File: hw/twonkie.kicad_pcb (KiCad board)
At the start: 4 copper layers, 25.4 x 25.4 mm, 55 parts, among them J1 DX07P024AJ1R1500, J2 690-024-294T331, J3 629105150521, Q1 BSD840N, Q2 BSD840N, Q3 BSD840N, SW1 EVQ-P7M01P, U1 INA260, U2 INA260, U3 MIC5504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

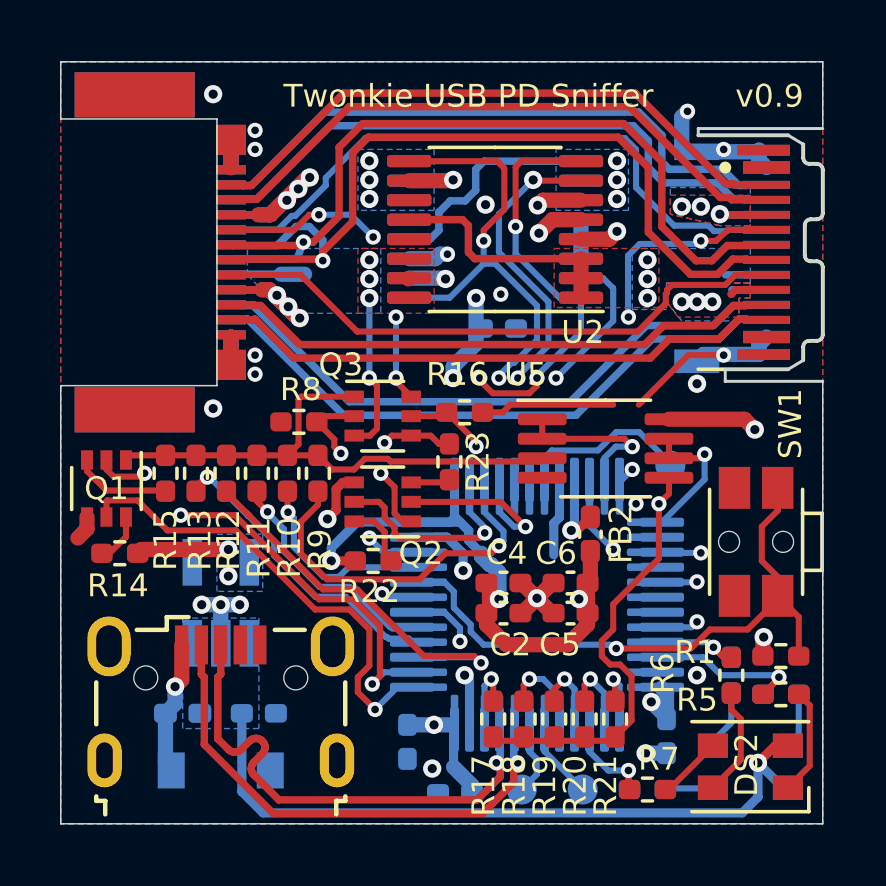
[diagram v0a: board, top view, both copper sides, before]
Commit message: Many reworks based on David's and Vincent's feedback
* The USB plug wouldn't straddle a 1.6mm board, so switched to
  a different one
* Redid the USB section to make room for the new plug
* Twinkie firmware needs some special pin functions I wasn't aware
  of, so some signals had to be moved to different pins
* Misc other tweaks like merging resistor values
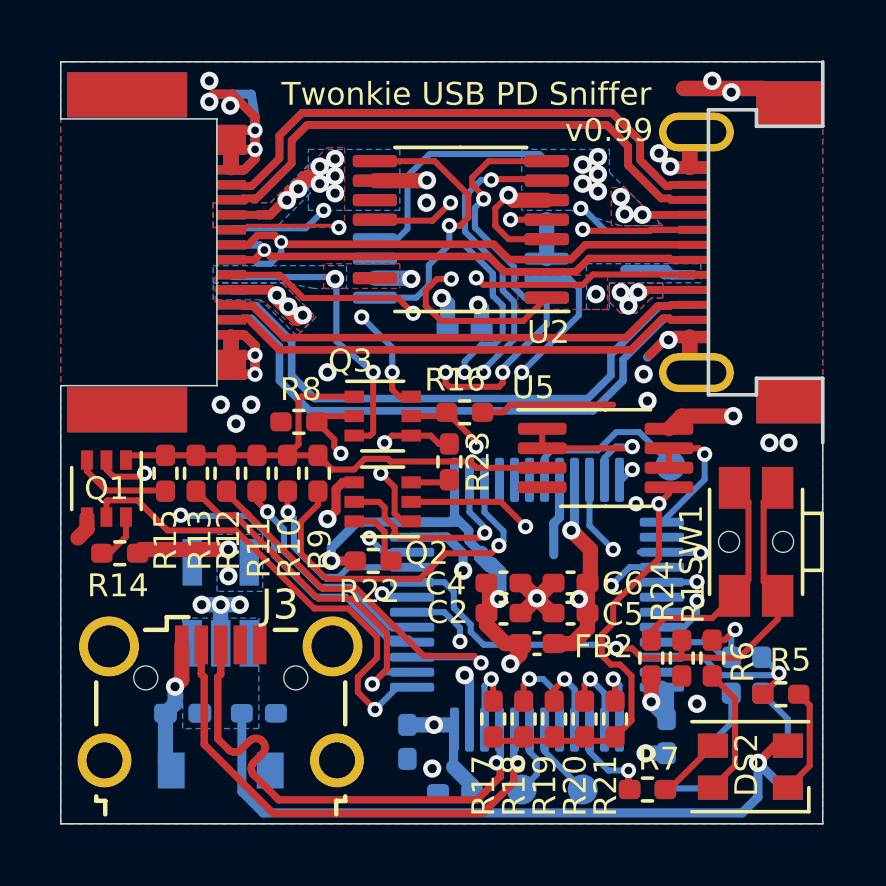
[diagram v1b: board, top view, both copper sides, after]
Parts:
- added R24: 100, Resistor_SMD:R_0402_1005Metric_Pad0.72x0.64mm_HandSolder, F.Cu at (91.6, 54.2)
- J1: value DX07P024AJ1R1500 -> USB4151; footprint twonkie:JAE_DX07P024AJ1R1500 -> twonkie:GCT_USB4151_EdgeMount
- J3: footprint Connector_USB:USB_Micro-B_Wuerth_629105150521 -> Connector_USB:USB_Micro-B_Wuerth_629105150521_CircularHoles
- R1: value 51k1 -> 35k7
- R16, R8: value 301k -> 35k7
- R2, R5: value 806 -> 390
- R3, R6: value 576 -> 240
- R4, R7: value 604 -> 240
- U4: value STM32F042C6 -> STM32F072CB; footprint twonkie:LQFP-48_7x7mm_P0.5mm-QFN48-Frankenstein -> Package_QFP:LQFP-48_7x7mm_P0.5mm
- moved FB2 4.06 mm to (87.8, 53.7), turned to 0 degrees
- moved J1 3.81 mm to (93.5, 40.6)
- moved R1 3.30 mm to (92.6, 54.2), turned to 270 degrees
- moved ? 2.62 mm to (78.0, 34.8)
- moved dojoe-logo 2.11 mm to (85.5, 45.5)
- moved C9 1.14 mm to (85.3, 43.2)
- moved U1 1.14 mm to (85.2, 39.9)
- moved U2 1.14 mm to (85.2, 39.9)
- moved R2 0.90 mm to (95.2, 54.7), turned to 90 degrees
- moved R6 0.85 mm to (93.6, 54.2)
- moved U5 0.32 mm to (90.0, 47.5)
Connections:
- C5 pad 1: +3V3 -> Net-(C5-Pad1)
- C6 pad 1: +3V3 -> Net-(C5-Pad1)
- FB2 pad 2: Net-(FB2-Pad2) -> Net-(C5-Pad1)
- R1 pad 1: +3V3 -> /BOOT
- R1 pad 2: /BOOT -> GND
- SW1 pad 1: GND -> Net-(R24-Pad2)
- U4 pad 16: Net-(U4-Pad16) -> /CC2_TX_DATA
- U4 pad 38: /CC1_TX_DATA -> /CC1_RPUSB
- U4 pad 4: /CC2_TX_DATA -> Net-(U4-Pad4)
- U4 pad 40: /CC1_RPUSB -> /CC1_TX_DATA
- U4 pad 9: Net-(FB2-Pad2) -> Net-(C5-Pad1)
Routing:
- net GND: track 40.9 -> 67.1 mm, vias 26 -> 33
- net /USBC_D-: track 28.6 -> 17.2 mm
- net /USBC_D+: track 27.0 -> 18.4 mm
- net Net-(R24-Pad2): track 0.00 -> 7.83 mm
- net /CC2_PLUG: track 9.46 -> 16.4 mm
- net Net-(C5-Pad1): track 0.00 -> 6.92 mm, vias 0 -> 2
- net /SBU2: track 22.8 -> 17.2 mm, vias 0 -> 2
- net /CC2_TX_DATA: track 6.30 -> 9.77 mm, vias 1 -> 2
- net /SBU1: track 19.7 -> 16.5 mm, vias 0 -> 2
- net /RX2+: track 18.9 -> 16.3 mm
- net /RX2-: track 18.9 -> 16.3 mm
- net Net-(FB2-Pad2): track 2.55 -> 0.00 mm, vias 1 -> 0
- net /TX_CLK: track 17.6 -> 15.4 mm
- net /CC1_RECEP: track 26.0 -> 23.8 mm, vias 6 -> 4
- net /INA_SDA: track 23.7 -> 25.8 mm
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- added copper zone on F.Cu, net /VBUS_RECEP
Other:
- outline, holes or cut-outs redrawn
- net class Diffpair: trace_width 0.24892 -> 0.254
- rule trace_min: 0.1524 -> 0.127
- rule via_min_size: 0.508 -> 0.4572
- board text added: "v0.99"
- board text removed: "v0.9"

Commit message: v0.99 with fabrication files
* Switch USB-MicroB receptacle to version with drill slots
* Expand VBUS connections on USB-C plug
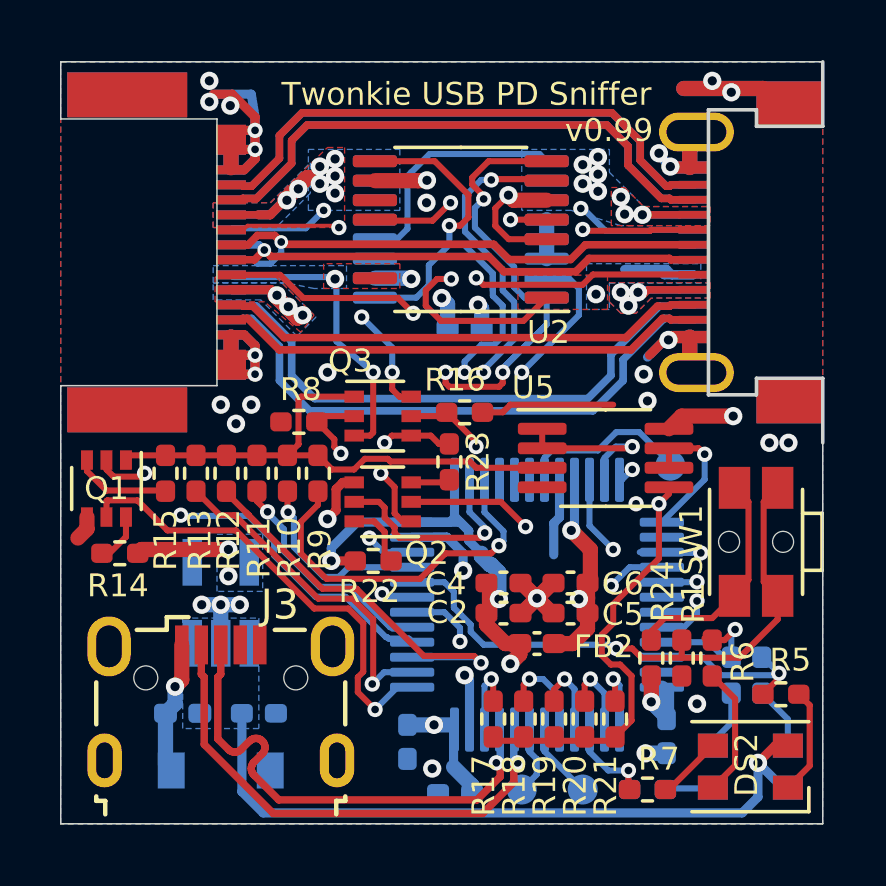
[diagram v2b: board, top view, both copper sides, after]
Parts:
- J3: footprint Connector_USB:USB_Micro-B_Wuerth_629105150521_CircularHoles -> Connector_USB:USB_Micro-B_Wuerth_629105150521

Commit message: First batch of v1.0 fixes
* Restore QFN/TQFP combo footprint for U4, make sure it stays
* Grow some VBUS copper pours
* Make U4 decap ground connections less solid for better soldering
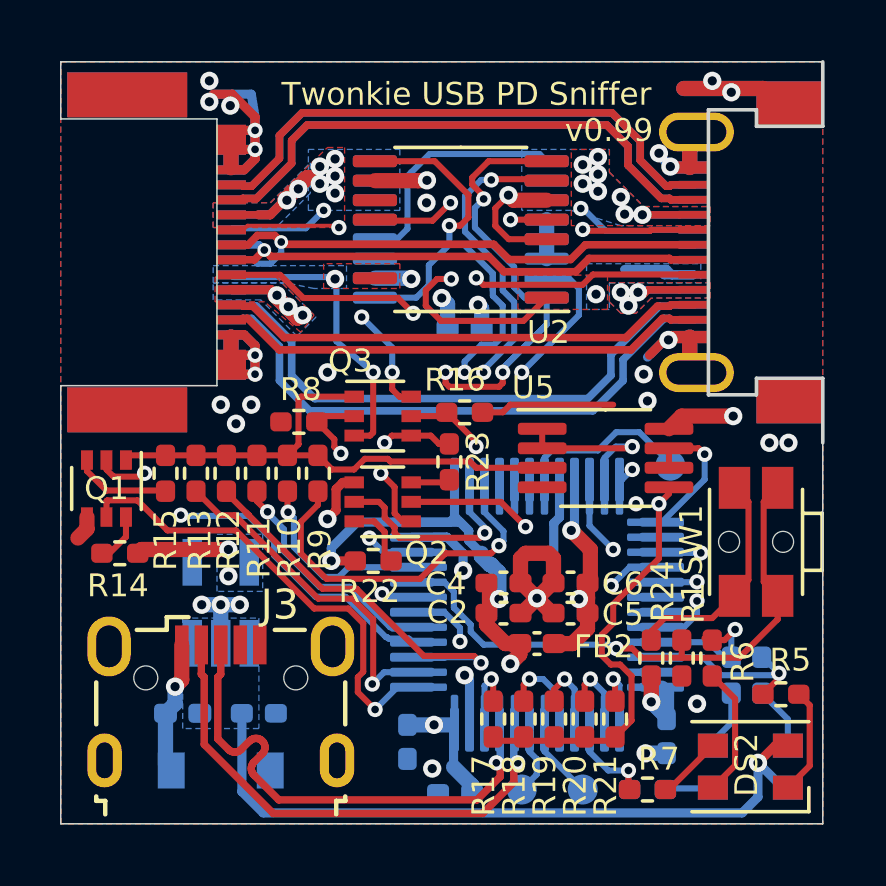
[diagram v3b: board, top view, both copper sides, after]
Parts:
- U4: footprint Package_QFP:LQFP-48_7x7mm_P0.5mm -> twonkie:LQFP-48_7x7mm_P0.5mm-QFN48-Frankenstein
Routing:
- net GND: track 67.1 -> 70.0 mm
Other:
- board text added: "TODO: Corner relief"

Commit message: Add relief to J2 cutout corners, update ground connections
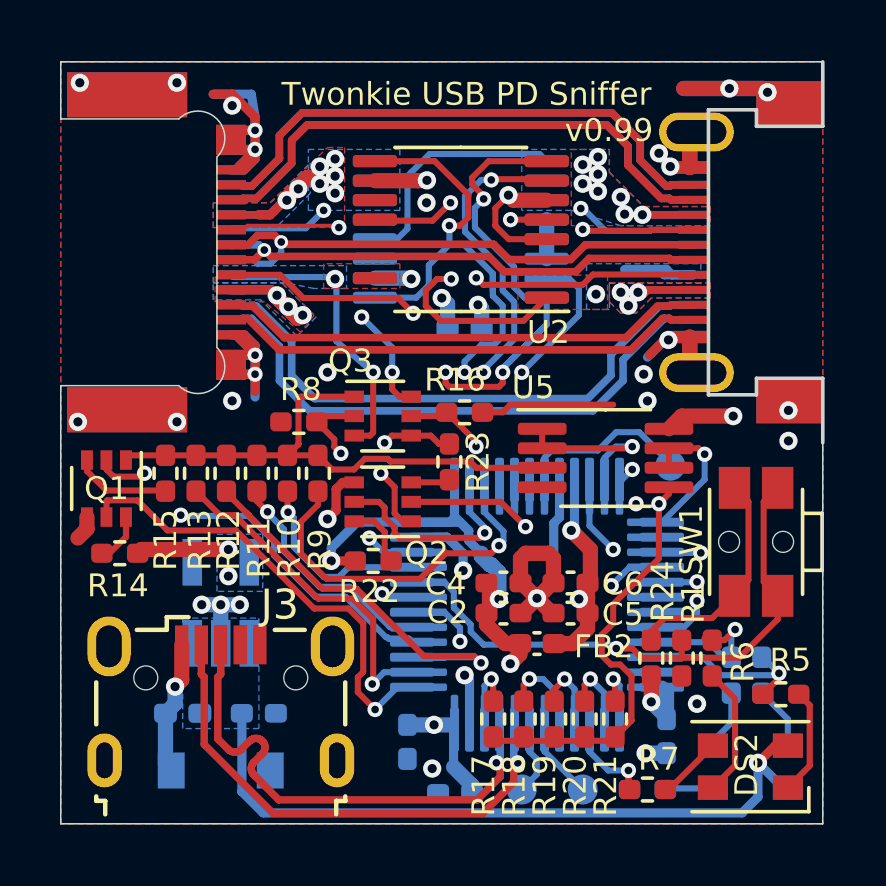
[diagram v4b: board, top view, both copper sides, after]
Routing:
- net GND: track 70.0 -> 68.4 mm
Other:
- outline, holes or cut-outs redrawn
- board text removed: "TODO: Corner relief"

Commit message: Add I2C pullup resistors
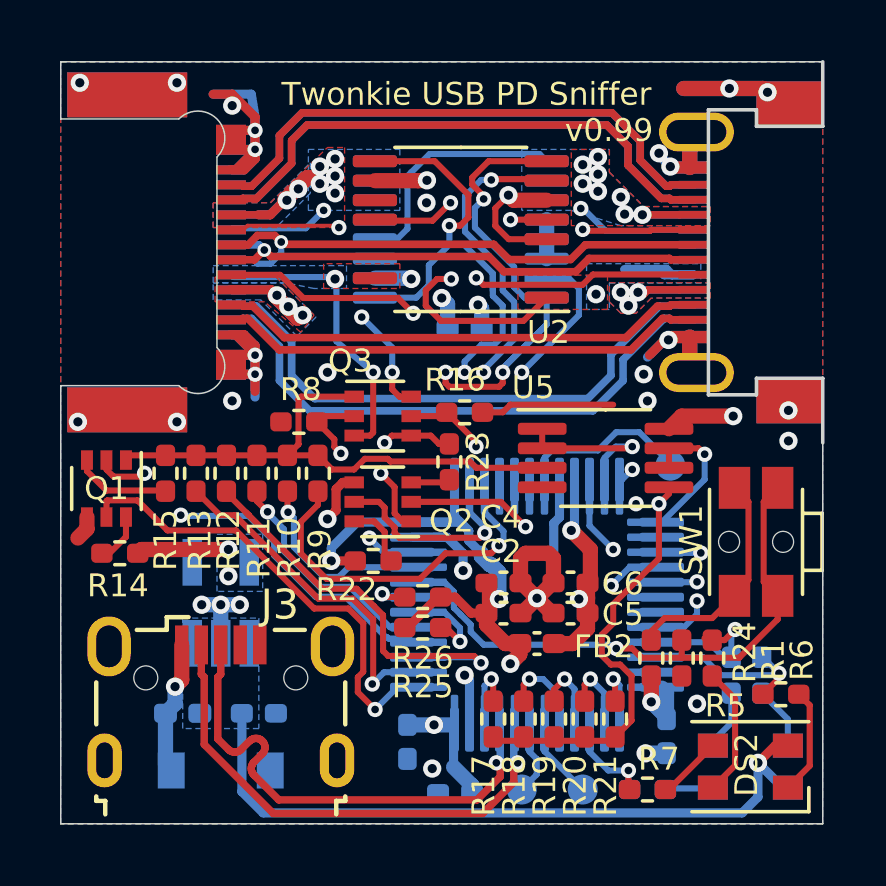
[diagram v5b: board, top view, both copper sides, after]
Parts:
- added R25: 4k75, Resistor_SMD:R_0402_1005Metric_Pad0.72x0.64mm_HandSolder, F.Cu at (83.9, 53.1)
- added R26: 4k75, Resistor_SMD:R_0402_1005Metric_Pad0.72x0.64mm_HandSolder, F.Cu at (83.9, 52.1)
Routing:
- net +3V3: track 43.4 -> 46.8 mm
- net /CC1_RD: track 13.4 -> 14.7 mm
- net /INA_SCL: track 29.3 -> 30.1 mm
- net /INA_SDA: track 25.8 -> 26.6 mm

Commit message: Improve C2/4/5/6 solderability
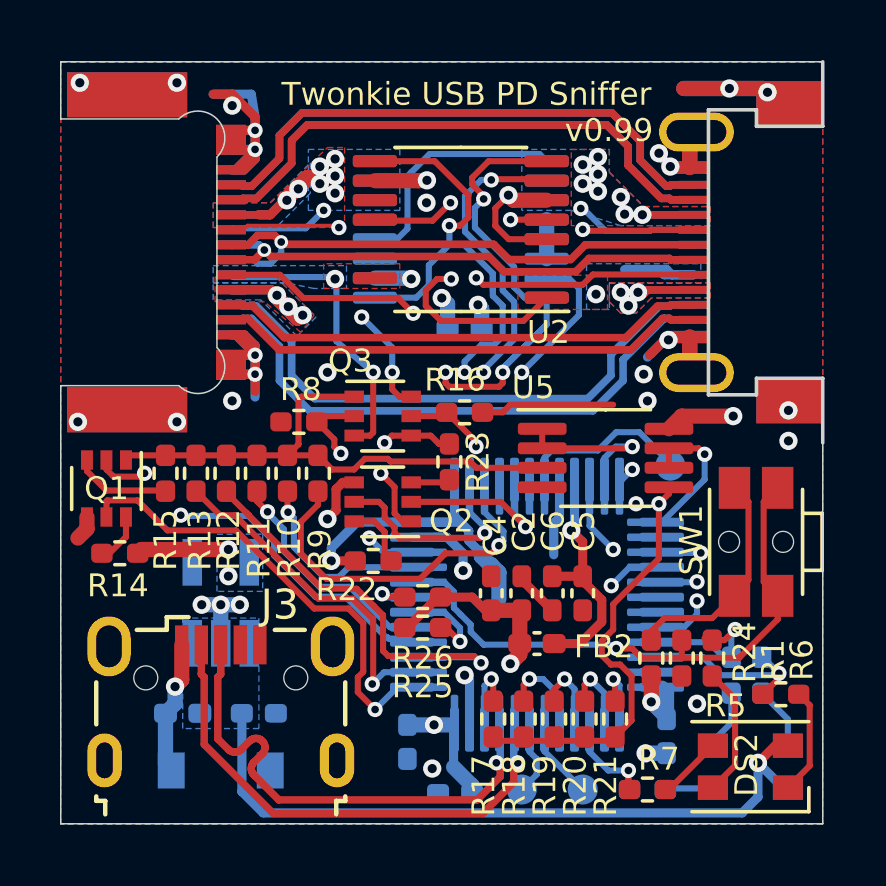
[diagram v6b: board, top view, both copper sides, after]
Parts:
- moved C2 0.90 mm to (87.2, 52.0), turned to 90 degrees
- moved C5 0.78 mm to (89.3, 52.0), turned to 270 degrees
- moved C6 0.70 mm to (88.3, 52.0), turned to 270 degrees
- moved C4 0.53 mm to (86.2, 52.0), turned to 90 degrees
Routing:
- net GND: track 68.4 -> 64.1 mm, vias 33 -> 32
- net +3V3: track 46.8 -> 45.0 mm, vias 13 -> 12
- net Net-(C5-Pad1): track 6.92 -> 8.10 mm, vias 2 -> 1

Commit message: Solderability improvememts around J3
* Extend J3 pads for easier hand soldering
* Move FB1, C1 to reach pads better
* Move J3 closer to board edge
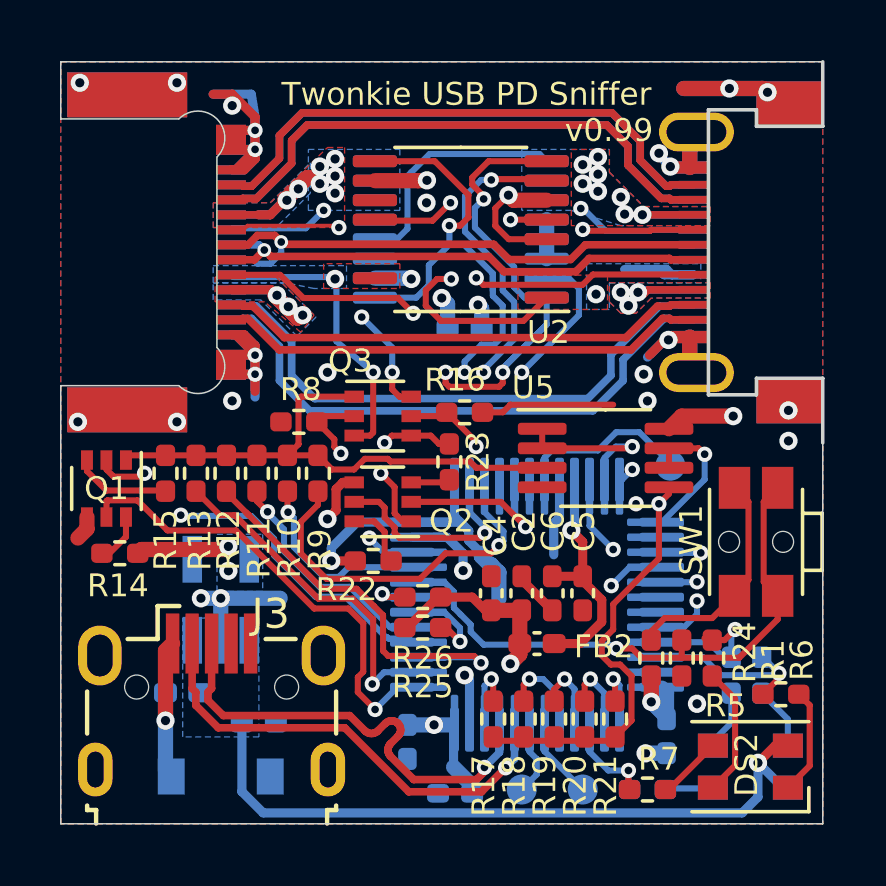
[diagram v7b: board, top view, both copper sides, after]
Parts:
- J3: footprint Connector_USB:USB_Micro-B_Wuerth_629105150521 -> twonkie:USB_Micro-B_Wuerth_629105150521_HandSolder
- moved FB1 0.69 mm to (75.9, 55.3)
- moved J3 0.43 mm to (76.9, 55.9)
- moved C1 0.33 mm to (78.5, 56.3)
- moved D1 0.20 mm to (77.2, 58.1)
- moved U3 0.10 mm to (77.2, 52.2)
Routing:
- net /USB_B_D-: track 16.9 -> 15.4 mm
- net /USB_B_D+: track 16.9 -> 15.4 mm
- net GND: track 64.1 -> 65.6 mm, vias 32 -> 30
- net Net-(D1-Pad1): track 4.49 -> 5.54 mm
